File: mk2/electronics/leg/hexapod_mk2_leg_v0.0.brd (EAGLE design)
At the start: 27 x 22.4 mm, 5 parts

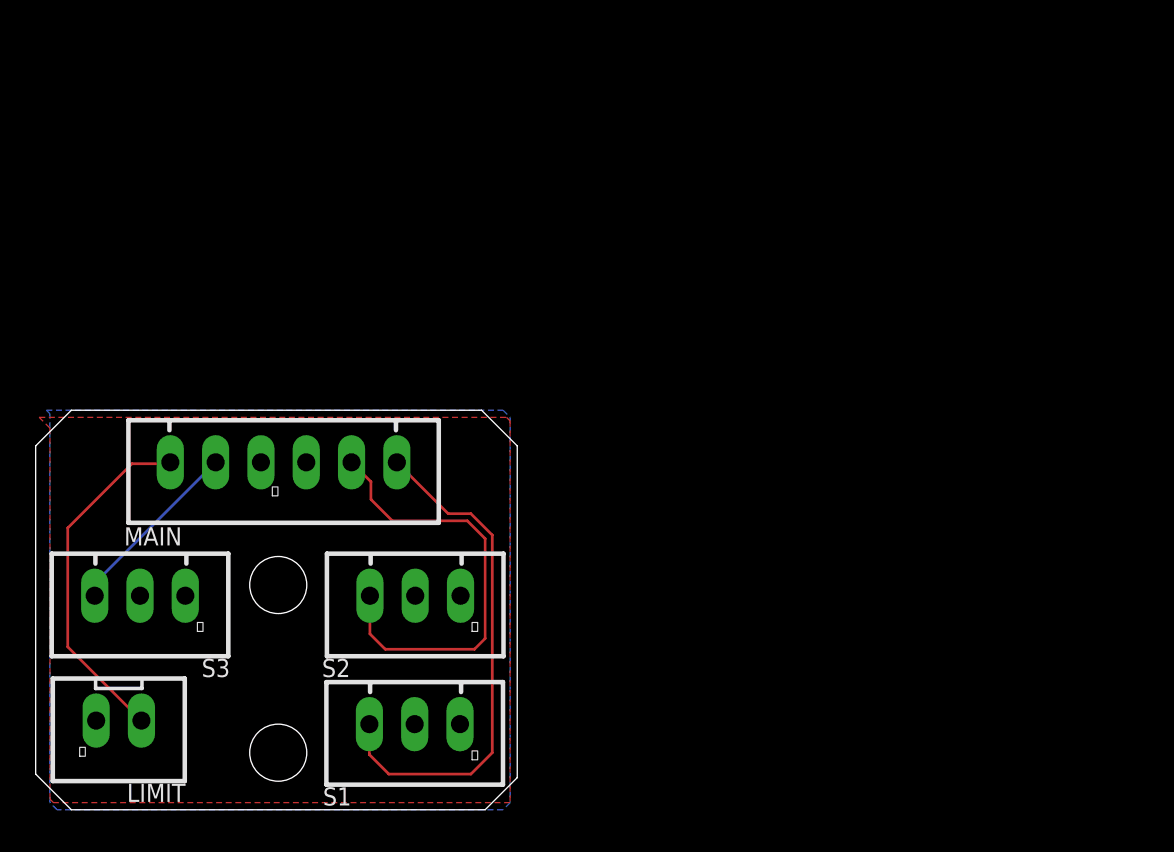
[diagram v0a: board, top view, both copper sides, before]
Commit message: servo decoupling caps
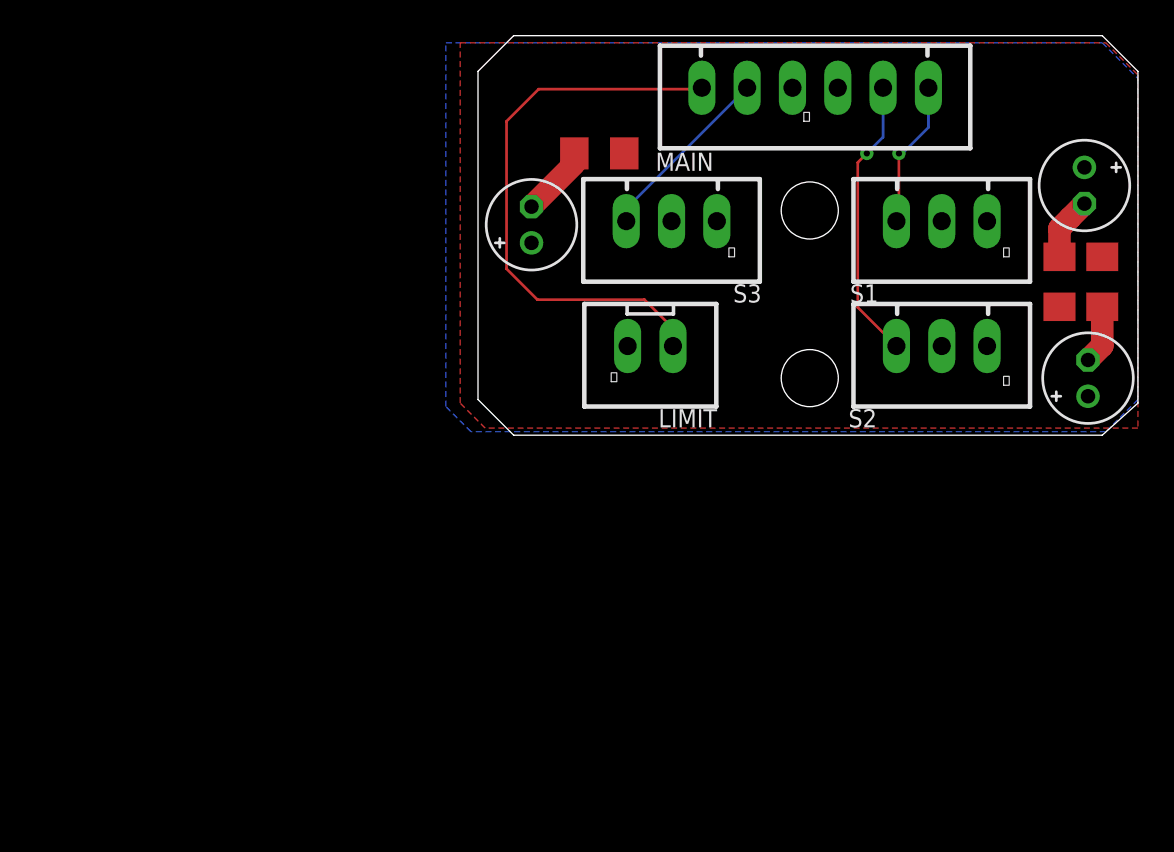
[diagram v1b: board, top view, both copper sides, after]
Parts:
- added C1, C2, C3: (no value), rcl:E2-5
- added C4, C5, C6: (no value), rcl:C1206
- moved S1 40.8 mm to (51.0, 33.6)
- moved S3 36.5 mm to (35.9, 33.6)
- moved LIMIT 36.5 mm to (34.7, 26.6)
- moved MAIN 36.5 mm to (43.9, 41.1)
- moved S2 32.7 mm to (51.0, 26.6)
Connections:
- net 5V: now also C1.+, C2.+, C3.+, C4.1, C5.1, C6.1
- net GND: now also C1.-, C2.-, C3.-, C4.2, C5.2, C6.2
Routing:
- net S1SIG: track 28.8 -> 8.34 mm, vias 0 -> 1
- net LIMIT: track 19.8 -> 31.7 mm
- net GND: track 0.00 -> 10.9 mm
- net S2SIG: track 24.6 -> 16.0 mm, vias 0 -> 1
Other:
- board size 27 x 22.4 mm -> 37 x 22.4 mm
- board text added: "Leg Breakout Mk 2, V1.1 June 2024"
- board text removed: "Leg Breakout Mk 2, V1.0 June 2024"
